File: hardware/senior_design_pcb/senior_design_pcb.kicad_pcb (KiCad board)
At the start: 4 copper layers, 290 x 202.5 mm, 60 parts, among them J1 SBH11-PBPC-D05-ST-BK, J10 1x06Screw-Stepper Driver2, J11 2x08Rectangle-LED Matrix Conn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, J12 1x05JST - Joystick2 connector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, J13 UJ20-C-H-C-4-SMT-TR, J3 1x02JST-IR Transmitter1, J4 1x03JST- IR Receiver1, J5 1x05JST-Admin LCD Console Con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, J6 1x05JST - Joystick1 connector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, J7 1x02JST-IR Transmitter, J8 1x03JST-IR Receiver2, J9 1x06Screw-Stepper Driver, SW3 1x02JST-Admin Console button 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, U2 STM32F091RCTx, U3 LD1117S33TR_SOT223, U4 KMR241GLFS

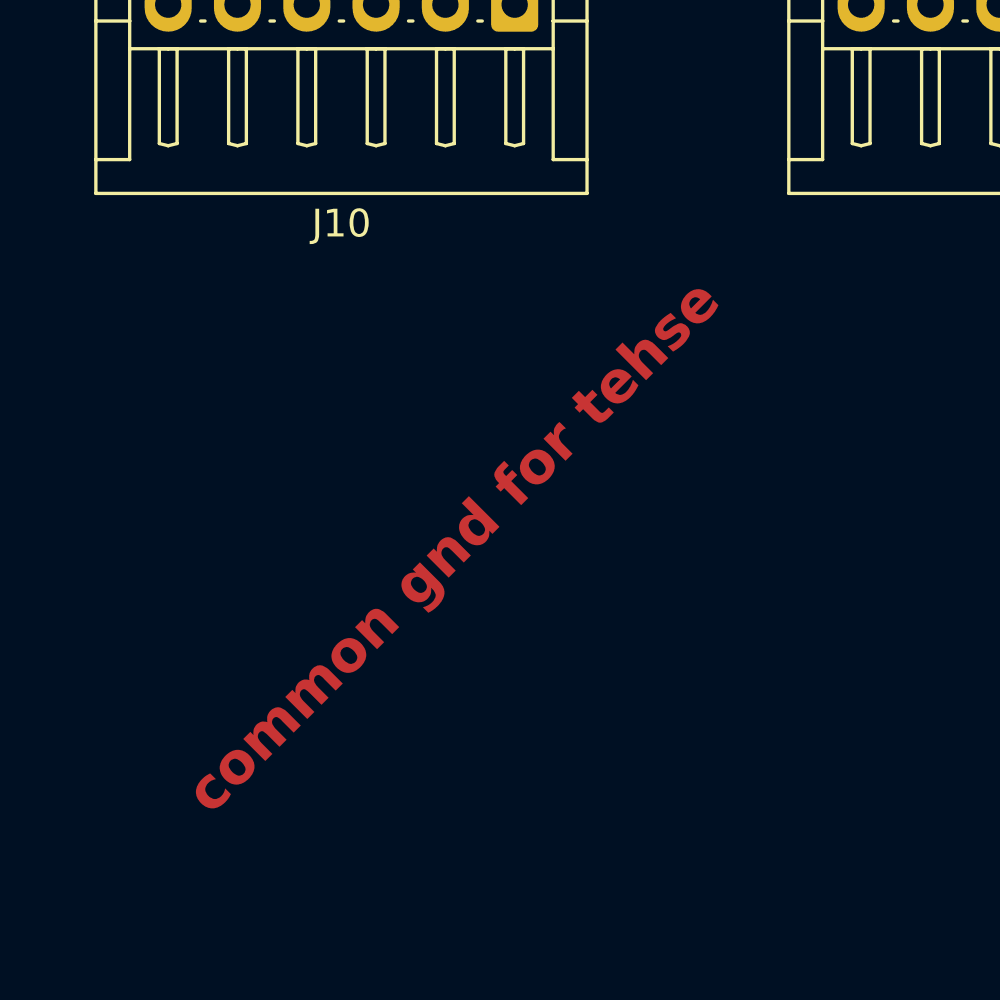
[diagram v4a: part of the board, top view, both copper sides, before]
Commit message: delete old files
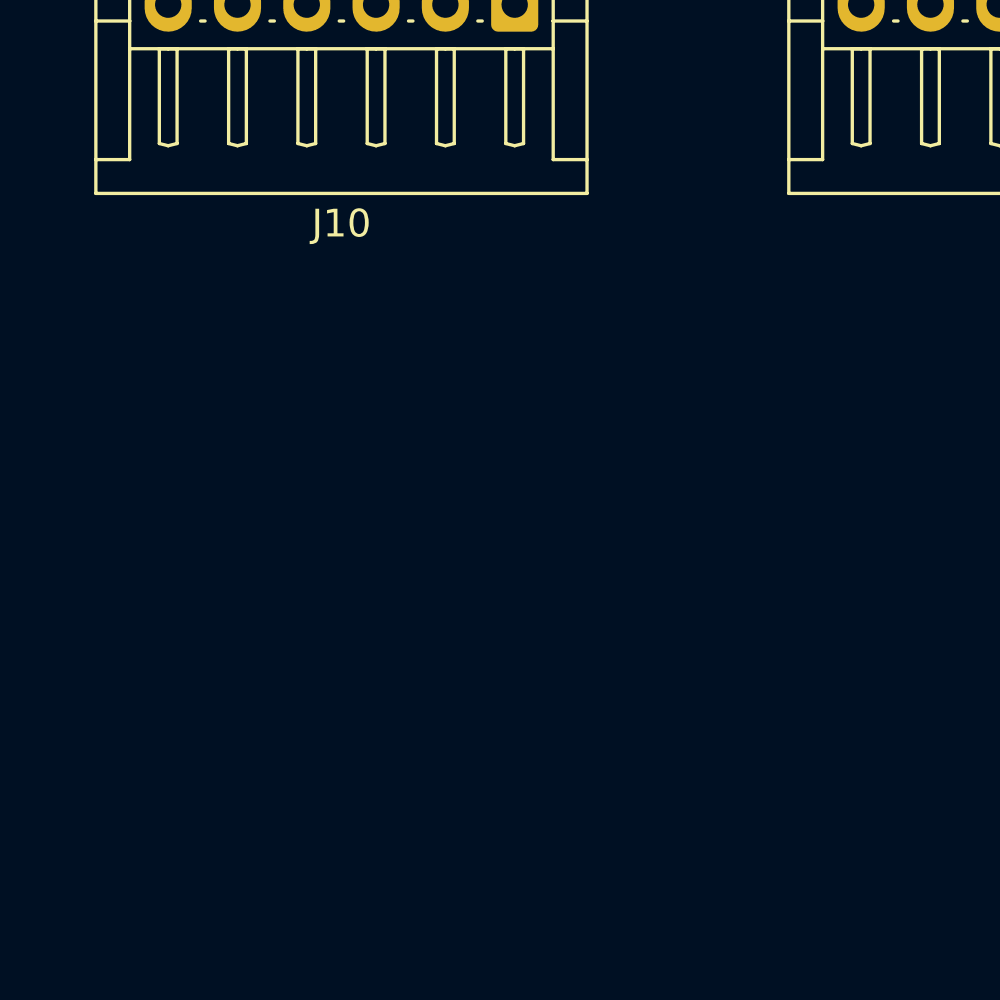
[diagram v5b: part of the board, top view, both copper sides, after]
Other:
- board text removed: "common gnd for tehse"
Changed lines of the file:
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@@
 		(layer "User.4")
-	)
-	(gr_text "common gnd for tehse"
-		(at 71.8 129.2 45)
-		(layer "F.Cu")
-		(effects
-			(font
-				(size 1.5 1.5)
-				(thickness 0.3)
-				(bold yes)
-			)
-			(justify left bottom)
-		)
 	)
 	(gr_text "the connectors are all 2.5 NOT 2.56mm rn"

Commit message: added comments
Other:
- board text added: "edge cuts is the whole area so that it stops throwing ground flywires. this is by no means the size we expect"
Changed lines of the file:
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@@
 		)
+	)
+	(gr_line
+		(start 165.6 52.6)
+		(end 167.262329 55.878813)
+		(stroke
+			(width 0.1)
+			(type default)
+		)
+		(layer "Cmts.User")
+	)
+	(gr_line
+		(start 165.6 52.6)
+		(end 169 52.6)
+		(stroke
+			(width 0.1)
+			(type default)
+		)
+		(layer "Cmts.User")
+	)
+	(gr_curve
+		(pts
+			(xy 172.2 87.4) (xy 180.8 69.6) (xy 170 54.6) (xy 167.8 53.6)
+		)
+		(stroke
+			(width 0.1)
+			(type default)
+		)
+		(layer "Cmts.User")
+	)
+	(gr_line
+		(start 143.6 104)
+		(end 143.6 108)
+		(stroke
+			(width 0.1)
+			(type default)
+		)
+		(layer "Cmts.User")
+	)
+	(gr_curve
+		(pts
+			(xy 167.8 53.6) (xy 165.6 52.6) (xy 165.6 52.6) (xy 165.6 52.6)
+		)
+		(stroke
+			(width 0.1)
+			(type default)
+		)
+		(layer "Cmts.User")
+	)
+	(gr_curve
+		(pts
+			(xy 156.4 95.6) (xy 156.4 103.6) (xy 148.8 106) (xy 144.8 106)
+		)
+		(stroke
+			(width 0.1)
+			(type default)
+		)
+		(layer "Cmts.User")
+	)
+	(gr_line
+		(start 140.8 106)
+		(end 143.6 104)
+		(stroke
+			(width 0.1)
+			(type default)
+		)
+		(layer "Cmts.User")
+	)
+	(gr_curve
+		(pts
+			(xy 144.8 106) (xy 140.8 106) (xy 140.8 106) (xy 140.8 106)
+		)
+		(stroke
+			(width 0.1)
+			(type default)
+		)
+		(layer "Cmts.User")
+	)
+	(gr_line
+		(start 167.262329 55.878813)
+		(end 165.6 52.6)
+		(stroke
+			(width 0.1)
+			(type default)
+		)
+		(layer "Cmts.User")
+	)
+	(gr_line
+		(start 143.6 108)
+		(end 140.8 106)
+		(stroke
+			(width 0.1)
+			(type default)
+		)
+		(layer "Cmts.User")
 	)
 	(gr_rect
@@
 	)
 	(gr_rect
-		(start 26.4 29.8)
-		(end 166.4 109.8)
+		(start 26.4 28.4)
+		(end 168.2 109.8)
 		(stroke
 			(width 0.1)
@@
 		(fill no)
 		(layer "User.4")
+	)
+	(gr_text "edge cuts is the whole area so that it stops throwing ground flywires. this is by no means the size we expect"
+		(at 162.6 6.6 0)
+		(layer "Cmts.User")
+		(effects
+			(font
+				(size 1.5 1.5)
+				(thickness 0.3)
+				(bold yes)
+			)
+			(justify left bottom)
+		)
 	)
 	(gr_text "the connectors are all 2.5 NOT 2.56mm rn"
@@
 		)
 	)
+	(gr_text_box "we will probably put some of these little .1uf on the other side for the sake of being able to route other traces"
+		(start 74.2 71.6)
+		(end 93.4 82)
+		(margins 1.0025 1.0025 1.0025 1.0025)
+		(layer "Cmts.User")
+		(effects
+			(font
+				(size 1 1)
+				(thickness 0.2)
+				(bold yes)
+			)
+			(justify left top)
+		)
+		(border yes)
+		(stroke
+			(width 0.2)
+			(type solid)
+		)
+	)
+	(gr_text_box "these are for stretch goals so they may or may not stay"
+		(start 156.4 87.6)
+		(end 174.4 95.6)
+		(margins 1.0025 1.0025 1.0025 1.0025)
+		(layer "Cmts.User")
+		(effects
+			(font
+				(size 1 1)
+				(thickness 0.2)
+				(bold yes)
+			)
+			(justify left top)
+		)
+		(border yes)
+		(stroke
+			(width 0.2)
+			(type solid)
+		)
+	)
+	(gr_text_box "this layout is likely to change. \n- the connectors dont have to be 90 degree angles.\n- we want to add extra pins to the STM "
+		(start 40.5 115.8)
+		(end 79.9 133)
+		(margins 1.0025 1.0025 1.0025 1.0025)
+		(layer "Cmts.User")
+		(effects
+			(font
+				(size 1.5 1.5)
+				(thickness 0.3)
+				(bold yes)
+			)
+			(justify left top)
+		)
+		(border yes)
+		(stroke
+			(width 0.2)
+			(type solid)
+		)
+	)
+	(gr_text_box "this clock setup is messy right now. hope to clean it up and talk to someone with more experience about the layout later"
+		(start 132.6 71.2)
+		(end 152.6 82)
+		(margins 1.0025 1.0025 1.0025 1.0025)
+		(layer "Cmts.User")
+		(effects
+			(font
+				(size 1 1)
+				(thickness 0.2)
+				(bold yes)
+			)
+			(justify left top)
+		)
+		(border yes)
+		(stroke
+			(width 0.2)
+			(type solid)
+		)
+	)

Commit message: test
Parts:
- moved C15 8.36 mm to (103.0, 74.0), turned to 180 degrees
- turned U2 to -135 degrees
